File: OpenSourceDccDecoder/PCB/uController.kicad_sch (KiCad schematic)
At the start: 10 parts, among them J3 ICSP, SW1 SW_SPST, U1 ATmega328-A, Y1 Crystal_GND2

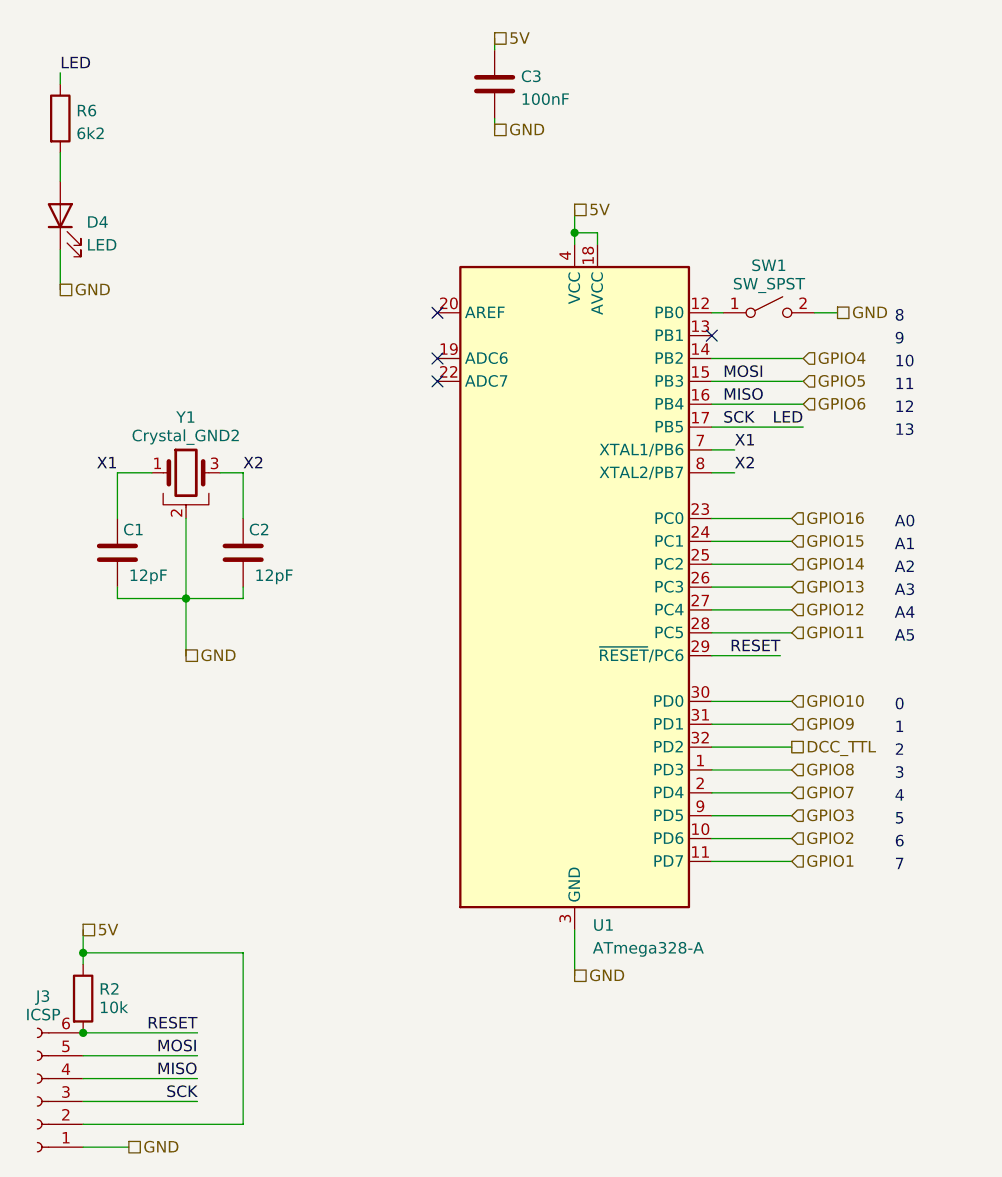
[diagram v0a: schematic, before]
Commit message: finalized routing on the Open source solenoid decoder
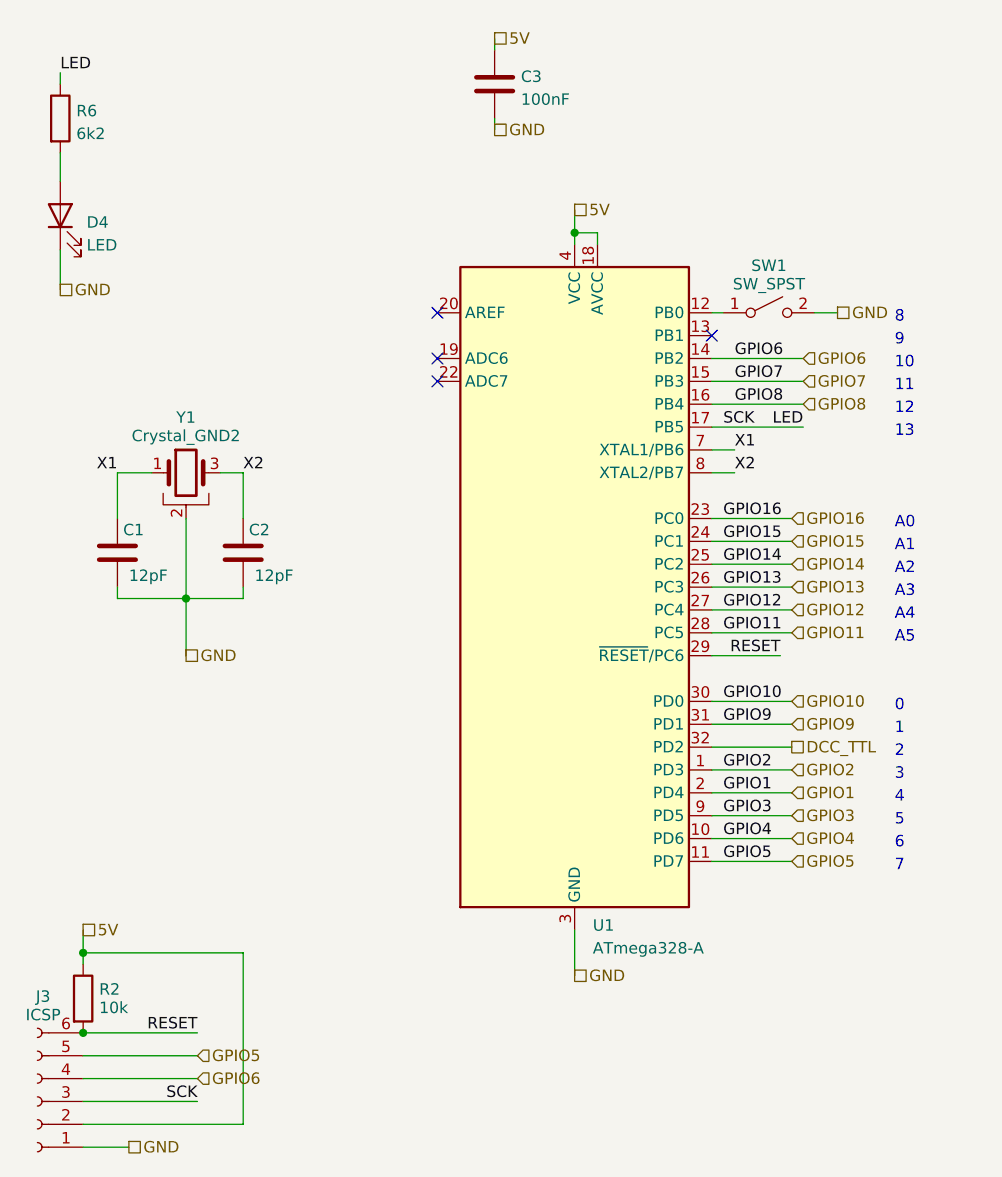
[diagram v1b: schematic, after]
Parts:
- J3: footprint (none) -> Connector_PinHeader_2.54mm:PinHeader_1x06_P2.54mm_Vertical
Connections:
- net GPIO1: now also U1.2 (PD4); no longer U1.11 (PD7)
- net GPIO2: now also U1.1 (PD3); no longer U1.10 (PD6)
- net GPIO4: now also U1.10 (PD6); no longer U1.14 (PB2)
- net GPIO5: now also U1.11 (PD7); no longer U1.15 (PB3)
- net GPIO6: now also U1.14 (PB2); no longer U1.16 (PB4)
- net GPIO7: now also U1.15 (PB3); no longer U1.2 (PD4)
- net GPIO8: now also U1.16 (PB4); no longer U1.1 (PD3)
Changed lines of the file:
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@@
     (stroke (width 0) (type default))
   )
-  (wire (pts (xy 114.3 116.84) (xy 105.41 116.84))
+  (wire (pts (xy 105.41 116.84) (xy 114.3 116.84))
     (stroke (width 0) (type default))
   )
@@
     (stroke (width 0) (type default))
   )
-  (wire (pts (xy 114.3 114.3) (xy 105.41 114.3))
+  (wire (pts (xy 105.41 114.3) (xy 114.3 114.3))
     (stroke (width 0) (type default))
   )
@@
     (stroke (width 0) (type default))
   )
-  (wire (pts (xy 114.3 111.76) (xy 105.41 111.76))
+  (wire (pts (xy 105.41 111.76) (xy 114.3 111.76))
     (stroke (width 0) (type default))
   )
@@
     (effects (font (size 1.27 1.27)) (justify left bottom))
   )
-  (label "MOSI" (at 48.26 138.43 180) (fields_autoplaced)
-    (effects (font (size 1.27 1.27)) (justify right bottom))
-  )
-  (label "MOSI" (at 106.68 63.5 0) (fields_autoplaced)
-    (effects (font (size 1.27 1.27)) (justify left bottom))
-  )
-  (label "MISO" (at 106.68 66.04 0) (fields_autoplaced)
+  (label "GPIO13" (at 106.68 86.36 0) (fields_autoplaced)
+    (effects (font (size 1.27 1.27)) (justify left bottom))
+  )
+  (label "GPIO8" (at 107.95 66.04 0) (fields_autoplaced)
+    (effects (font (size 1.27 1.27)) (justify left bottom))
+  )
+  (label "GPIO1" (at 106.68 109.22 0) (fields_autoplaced)
+    (effects (font (size 1.27 1.27)) (justify left bottom))
+  )
+  (label "GPIO16" (at 106.68 78.74 0) (fields_autoplaced)
+    (effects (font (size 1.27 1.27)) (justify left bottom))
+  )
+  (label "GPIO14" (at 106.68 83.82 0) (fields_autoplaced)
     (effects (font (size 1.27 1.27)) (justify left bottom))
   )
@@
     (effects (font (size 1.27 1.27)) (justify left bottom))
   )
+  (label "GPIO2" (at 106.68 106.68 0) (fields_autoplaced)
+    (effects (font (size 1.27 1.27)) (justify left bottom))
+  )
+  (label "GPIO15" (at 106.68 81.28 0) (fields_autoplaced)
+    (effects (font (size 1.27 1.27)) (justify left bottom))
+  )
   (label "SCK" (at 106.68 68.58 0) (fields_autoplaced)
     (effects (font (size 1.27 1.27)) (justify left bottom))
   )
   (label "X1" (at 107.95 71.12 0) (fields_autoplaced)
+    (effects (font (size 1.27 1.27)) (justify left bottom))
+  )
+  (label "GPIO10" (at 106.68 99.06 0) (fields_autoplaced)
     (effects (font (size 1.27 1.27)) (justify left bottom))
   )
@@
     (effects (font (size 1.27 1.27)) (justify right bottom))
   )
-  (label "MISO" (at 48.26 140.97 180) (fields_autoplaced)
-    (effects (font (size 1.27 1.27)) (justify right bottom))
-  )
   (label "LED" (at 115.57 68.58 180) (fields_autoplaced)
     (effects (font (size 1.27 1.27)) (justify right bottom))
@@
     (effects (font (size 1.27 1.27)) (justify right bottom))
   )
-  (hierarchical_label "GPIO2" (shape input) (at 114.3 114.3 0) (fields_autoplaced)
+  (label "GPIO3" (at 106.68 111.76 0) (fields_autoplaced)
+    (effects (font (size 1.27 1.27)) (justify left bottom))
+  )
+  (label "GPIO5" (at 106.68 116.84 0) (fields_autoplaced)
+    (effects (font (size 1.27 1.27)) (justify left bottom))
+  )
+  (label "GPIO9" (at 106.68 101.6 0) (fields_autoplaced)
+    (effects (font (size 1.27 1.27)) (justify left bottom))
+  )
+  (label "GPIO11" (at 106.68 91.44 0) (fields_autoplaced)
+    (effects (font (size 1.27 1.27)) (justify left bottom))
+  )
+  (label "GPIO7" (at 107.95 63.5 0) (fields_autoplaced)
+    (effects (font (size 1.27 1.27)) (justify left bottom))
+  )
+  (label "GPIO6" (at 107.95 60.96 0) (fields_autoplaced)
+    (effects (font (size 1.27 1.27)) (justify left bottom))
+  )
+  (label "GPIO4" (at 106.68 114.3 0) (fields_autoplaced)
+    (effects (font (size 1.27 1.27)) (justify left bottom))
+  )
+  (label "GPIO12" (at 106.68 88.9 0) (fields_autoplaced)
+    (effects (font (size 1.27 1.27)) (justify left bottom))
+  )
+  (hierarchical_label "GPIO8" (shape input) (at 115.57 66.04 0) (fields_autoplaced)
     (effects (font (size 1.27 1.27)) (justify left))
   )
@@
     (effects (font (size 1.27 1.27)) (justify left))
   )
+  (hierarchical_label "GPIO13" (shape input) (at 114.3 86.36 0) (fields_autoplaced)
+    (effects (font (size 1.27 1.27)) (justify left))
+  )
+  (hierarchical_label "GND" (shape passive) (at 46.99 93.98 0) (fields_autoplaced)
+    (effects (font (size 1.27 1.27)) (justify left))
+  )
+  (hierarchical_label "GPIO14" (shape input) (at 114.3 83.82 0) (fields_autoplaced)
+    (effects (font (size 1.27 1.27)) (justify left))
+  )
   (hierarchical_label "GPIO3" (shape input) (at 114.3 111.76 0) (fields_autoplaced)
     (effects (font (size 1.27 1.27)) (justify left))
   )
-  (hierarchical_label "GPIO13" (shape input) (at 114.3 86.36 0) (fields_autoplaced)
-    (effects (font (size 1.27 1.27)) (justify left))
-  )
-  (hierarchical_label "GND" (shape passive) (at 46.99 93.98 0) (fields_autoplaced)
-    (effects (font (size 1.27 1.27)) (justify left))
-  )
-  (hierarchical_label "GPIO14" (shape input) (at 114.3 83.82 0) (fields_autoplaced)
-    (effects (font (size 1.27 1.27)) (justify left))
-  )
-  (hierarchical_label "GPIO4" (shape input) (at 115.57 60.96 0) (fields_autoplaced)
-    (effects (font (size 1.27 1.27)) (justify left))
-  )
-  (hierarchical_label "GPIO8" (shape input) (at 114.3 106.68 0) (fields_autoplaced)
+  (hierarchical_label "GPIO4" (shape input) (at 114.3 114.3 0) (fields_autoplaced)
     (effects (font (size 1.27 1.27)) (justify left))
   )
@@
     (effects (font (size 1.27 1.27)) (justify left))
   )
+  (hierarchical_label "GPIO6" (shape input) (at 115.57 60.96 0) (fields_autoplaced)
+    (effects (font (size 1.27 1.27)) (justify left))
+  )
   (hierarchical_label "GPIO10" (shape input) (at 114.3 99.06 0) (fields_autoplaced)
     (effects (font (size 1.27 1.27)) (justify left))
@@
     (effects (font (size 1.27 1.27)) (justify left))
   )
-  (hierarchical_label "GPIO1" (shape input) (at 114.3 116.84 0) (fields_autoplaced)
-    (effects (font (size 1.27 1.27)) (justify left))
-  )
   (hierarchical_label "5V" (shape passive) (at 81.28 25.4 0) (fields_autoplaced)
     (effects (font (size 1.27 1.27)) (justify left))
   )
-  (hierarchical_label "GPIO6" (shape input) (at 115.57 66.04 0) (fields_autoplaced)
+  (hierarchical_label "GPIO5" (shape input) (at 114.3 116.84 0) (fields_autoplaced)
+    (effects (font (size 1.27 1.27)) (justify left))
+  )
+  (hierarchical_label "GPIO1" (shape input) (at 114.3 109.22 0) (fields_autoplaced)
+    (effects (font (size 1.27 1.27)) (justify left))
+  )
+  (hierarchical_label "GPIO2" (shape input) (at 114.3 106.68 0) (fields_autoplaced)
     (effects (font (size 1.27 1.27)) (justify left))
   )
@@
     (effects (font (size 1.27 1.27)) (justify left))
   )
+  (hierarchical_label "GPIO5" (shape input) (at 48.26 138.43 0) (fields_autoplaced)
+    (effects (font (size 1.27 1.27)) (justify left))
+  )
+  (hierarchical_label "GPIO7" (shape input) (at 115.57 63.5 0) (fields_autoplaced)
+    (effects (font (size 1.27 1.27)) (justify left))
+  )
   (hierarchical_label "GND" (shape passive) (at 90.17 129.54 0) (fields_autoplaced)
     (effects (font (size 1.27 1.27)) (justify left))
@@
     (effects (font (size 1.27 1.27)) (justify left))
   )
-  (hierarchical_label "GPIO7" (shape input) (at 114.3 109.22 0) (fields_autoplaced)
-    (effects (font (size 1.27 1.27)) (justify left))
-  )
   (hierarchical_label "GPIO15" (shape input) (at 114.3 81.28 0) (fields_autoplaced)
     (effects (font (size 1.27 1.27)) (justify left))
   )
-  (hierarchical_label "GPIO5" (shape input) (at 115.57 63.5 0) (fields_autoplaced)
-    (effects (font (size 1.27 1.27)) (justify left))
-  )
   (hierarchical_label "GPIO16" (shape input) (at 114.3 78.74 0) (fields_autoplaced)
     (effects (font (size 1.27 1.27)) (justify left))
   )
   (hierarchical_label "GND" (shape passive) (at 81.28 35.56 0) (fields_autoplaced)
+    (effects (font (size 1.27 1.27)) (justify left))
+  )
+  (hierarchical_label "GPIO6" (shape input) (at 48.26 140.97 0) (fields_autoplaced)
     (effects (font (size 1.27 1.27)) (justify left))
   )
@@
       (effects (font (size 1.27 1.27)))
     )
-    (property "Footprint" "" (at 30.48 143.51 0)
-      (effects (font (size 1.27 1.27)) hide)
-    )
+    (property "Footprint" "Connector_PinHeader_2.54mm:PinHeader_1x06_P2.54mm_Vertical" (at 30.48 143.51 0)
+      (effects (font (size 1.27 1.27)) hide)
+    )

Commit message: some dcc decoder work done. screw terminals need some spacing so I get 4 groups of 6 terminals. I need solder pads underneath the rectifier for the event it dies or more current is needed.
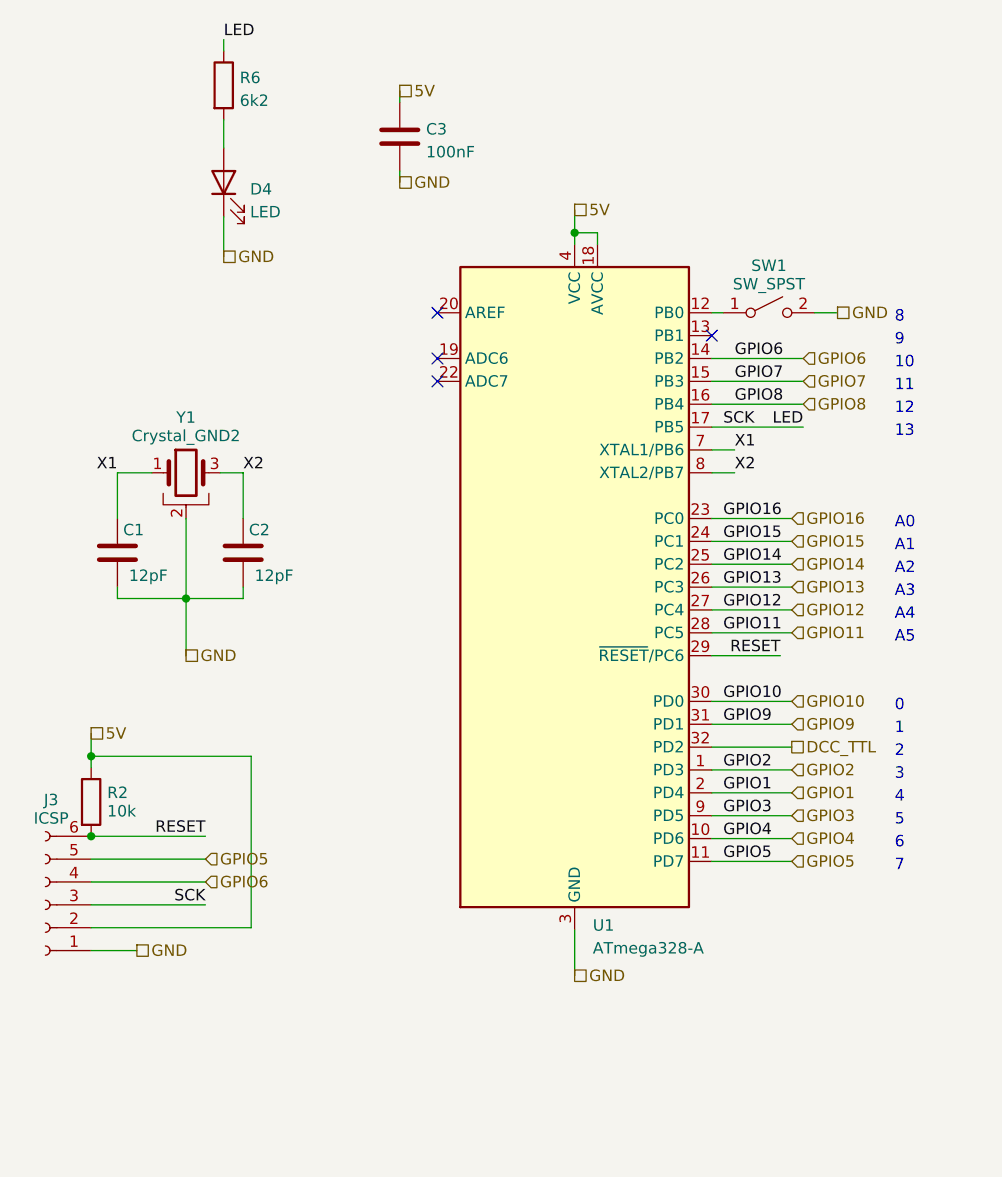
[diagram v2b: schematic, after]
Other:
- moved on the sheet: C3, D4, J3, R2, R6

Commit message: added missing files. Mostly  OSSD stuff
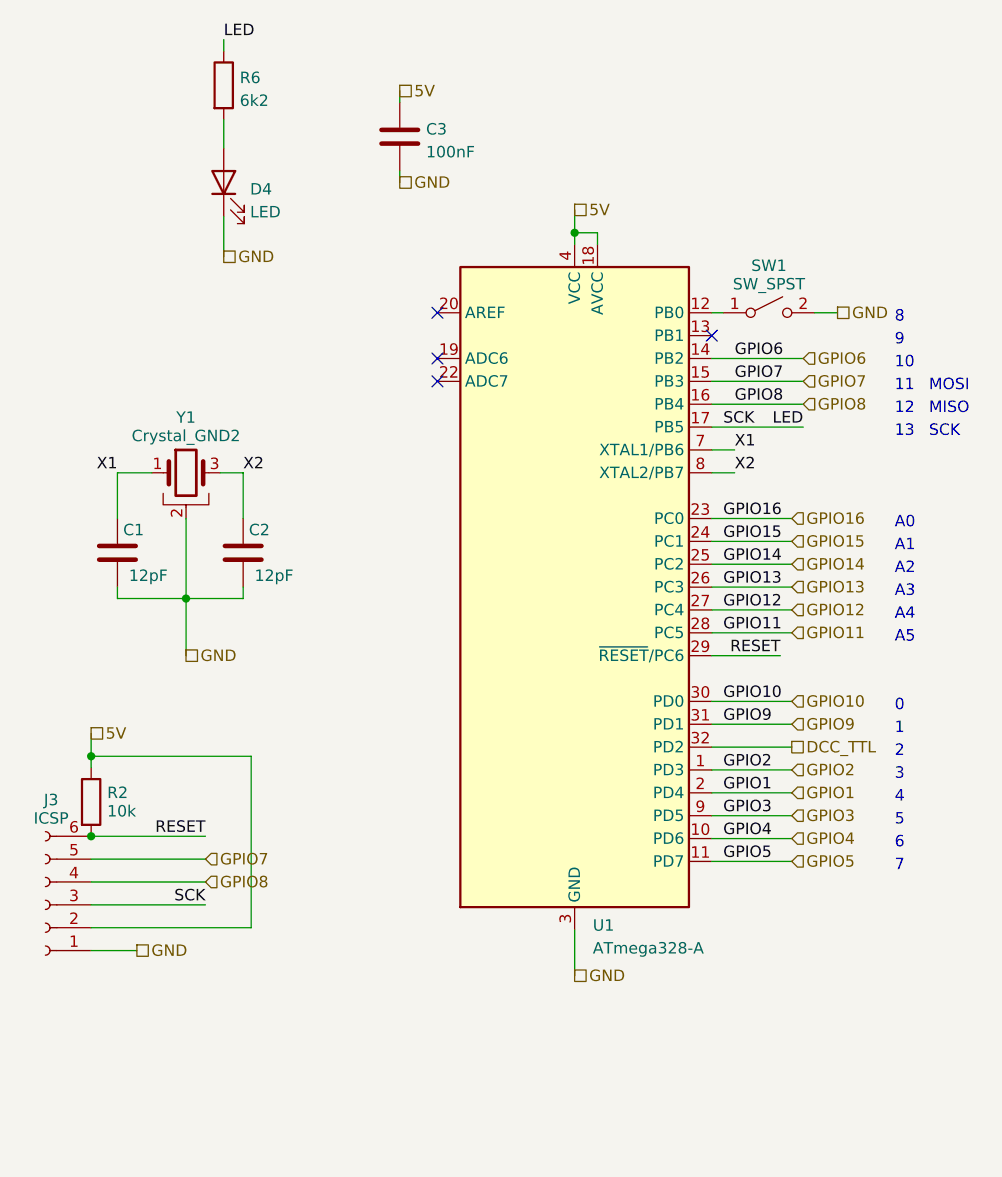
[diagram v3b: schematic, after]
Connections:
- net GPIO5: no longer J3.5 (Pin_5)
- net GPIO6: no longer J3.4 (Pin_4)
- net GPIO7: now also J3.5 (Pin_5)
- net GPIO8: now also J3.4 (Pin_4)
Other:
- note added: "MISO"
- note added: "MOSI"
- note added: "SCK"
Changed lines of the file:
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@@
+    (effects (font (size 1.27 1.27)) (justify left bottom))
+  )
+  (text "MOSI" (at 129.54 64.77 0)
     (effects (font (size 1.27 1.27)) (justify left bottom))
   )
@@
     (effects (font (size 1.27 1.27)) (justify left bottom))
   )
+  (text "SCK" (at 129.54 69.85 0)
+    (effects (font (size 1.27 1.27)) (justify left bottom))
+  )
+  (text "MISO" (at 129.54 67.31 0)
+    (effects (font (size 1.27 1.27)) (justify left bottom))
+  )
   (text "A3" (at 125.73 87.63 0)
     (effects (font (size 1.27 1.27)) (justify left bottom))
@@
     (effects (font (size 1.27 1.27)) (justify left))
   )
-  (hierarchical_label "GPIO5" (shape input) (at 49.149 116.586 0) (fields_autoplaced)
+  (hierarchical_label "GPIO7" (shape input) (at 49.149 116.586 0) (fields_autoplaced)
     (effects (font (size 1.27 1.27)) (justify left))
   )
@@
     (effects (font (size 1.27 1.27)) (justify left))
   )
-  (hierarchical_label "GPIO6" (shape input) (at 49.149 119.126 0) (fields_autoplaced)
-    (effects (font (size 1.27 1.27)) (justify left))
-  )
+  (hierarchical_label "GPIO8" (shape input) (at 49.149 119.126 0) (fields_autoplaced)
+    (effects (font (size 1.27 1.27)) (justify left))
+  )
